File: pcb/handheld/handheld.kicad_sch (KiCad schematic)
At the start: 64 parts, among them J1 Battery, J2 USB_C_Receptacle_USB2.0_16P, J3 Display Output, J4 Speaker ~(3W, 8R), J5 Joystick, J6 Debug, Q1 MMBT3904, SW1 SLW-1678105-6A-N-D, SW10 R, SW2 Reset, SW3 Boot, SW4 Select, SW5 A, SW6 B, SW7 X, SW8 Y, SW9 L, U1 ESP32-S3-WROOM-1, U2 AMS1117-3.3

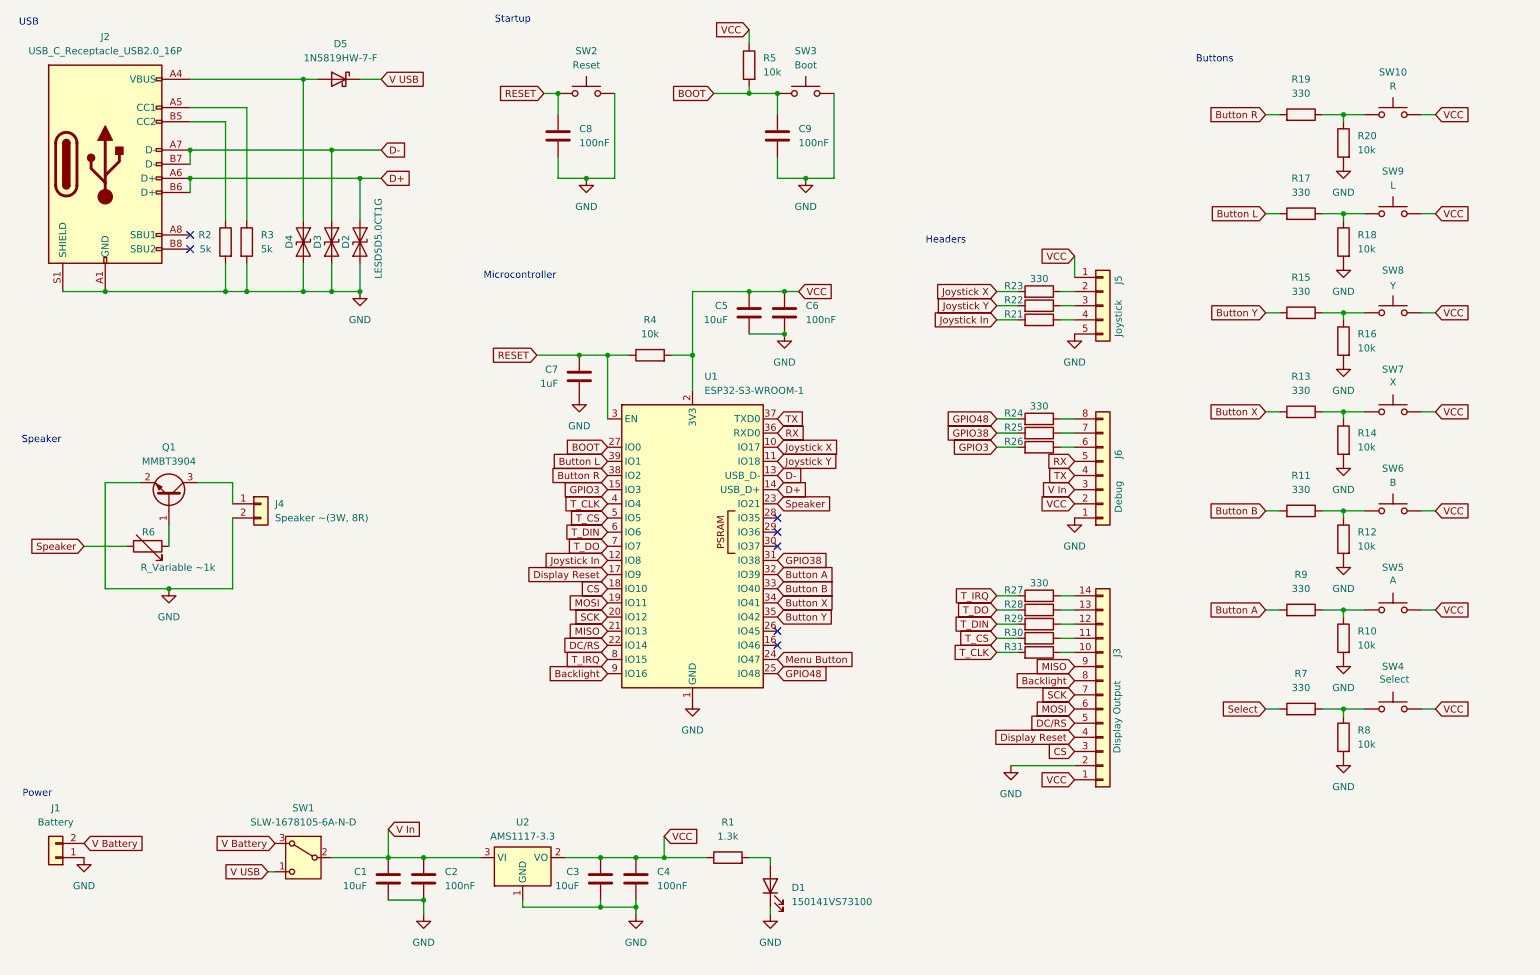
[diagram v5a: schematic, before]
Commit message: Updated symbols and footprints mainly
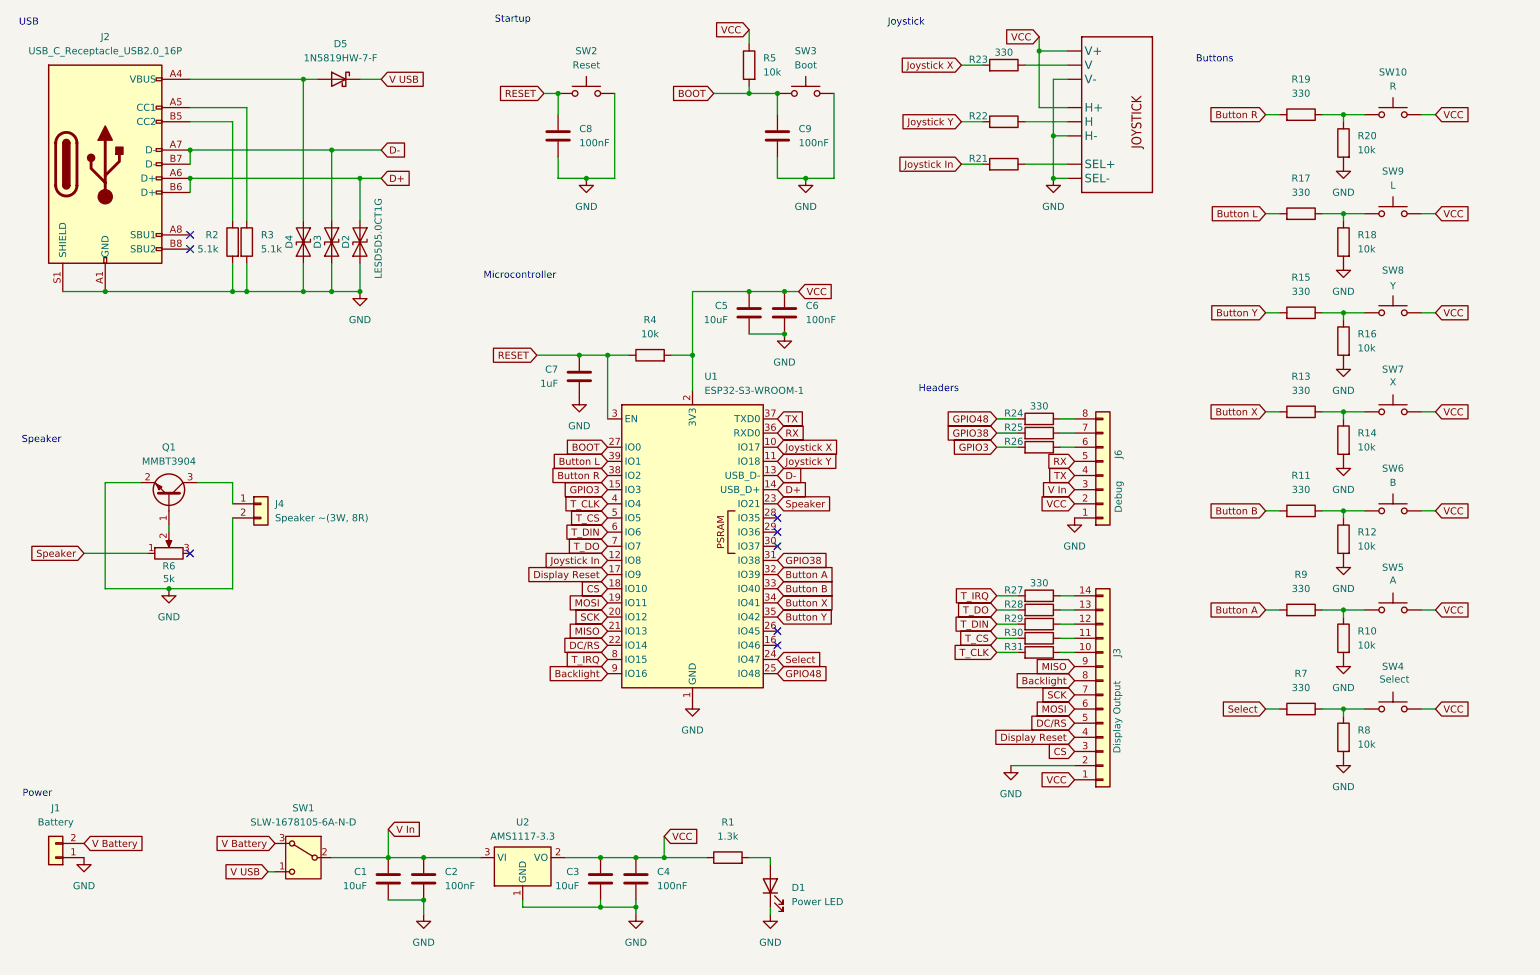
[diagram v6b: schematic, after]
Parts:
- removed J5: Joystick, symbol Connector_Generic:Conn_01x05
- removed R6: R_Variable ~1k, symbol Device:R_Variable
- added R6: 5k, handheld:RES-ADJ-TH_3P-L6.6-W7.0-P2.54-L_3362P, symbol Device:R_Potentiometer
- added U3: ~, handheld:JOYSTICK, symbol handheld_symbols:JOYSTICKPTH
- C1, C2, C3, C4, C5, C6, C7, C8, C9: footprint (none) -> Capacitor_SMD:C_0805_2012Metric
- D1: value 150141VS73100 -> Power LED; footprint (none) -> LED_SMD:LED_0603_1608Metric
- D5: footprint Diode_THT:D_DO-41_SOD81_P10.16mm_Horizontal -> Diode_SMD:D_SOD-123
- J1, J4: footprint (none) -> Connector_PinSocket_2.54mm:PinSocket_1x02_P2.54mm_Horizontal
- J2: footprint (none) -> handheld:USB-SMD_USB-TYPE-C-020
- J3: footprint (none) -> Connector_PinHeader_2.54mm:PinHeader_1x14_P2.54mm_Horizontal
- J6: footprint (none) -> Connector_PinSocket_2.54mm:PinSocket_1x08_P2.54mm_Vertical
- R1, R10, R11, R12, R13, R14, R15, R16, R17, R18, R19, R20, R21, R22, R23, R24, R25, R26, R27, R28, R29, R30, R31, R4, R5, R7, R8, R9: footprint (none) -> Resistor_SMD:R_0805_2012Metric
- R2, R3: value 5k -> 5.1k; footprint (none) -> Resistor_SMD:R_0805_2012Metric
- SW1: footprint Button_Switch_SMD:Nidec_Copal_CAS-120A -> handheld:SW_SLW-1678105-6A-N-D
- SW10, SW2, SW3, SW4, SW5, SW6, SW7, SW8, SW9: footprint (none) -> Button_Switch_THT:SW_TH_Tactile_Omron_B3F-100x
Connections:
- net Menu Button is gone; now on net Select: U1.24 (IO47)
- net GND: now also U3.B2A (SEL-), U3.H3 (H-), U3.V3 (V-)
- net Speaker: now also R6.1
- net VCC: now also U3.H1 (H+), U3.V1 (V+)
- net at Q1.1 (B): now also R6.2
- net at R22.1: now also U3.H2 (H)
- net at R23.1: now also U3.V2 (V)
- net at R21.1: now also U3.B1A (SEL+)
- no-connect marks 7 -> 8
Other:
- note added: "Joystick"
- moved on the sheet: R2, R21, R22, R23

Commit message: Initial PCB routing
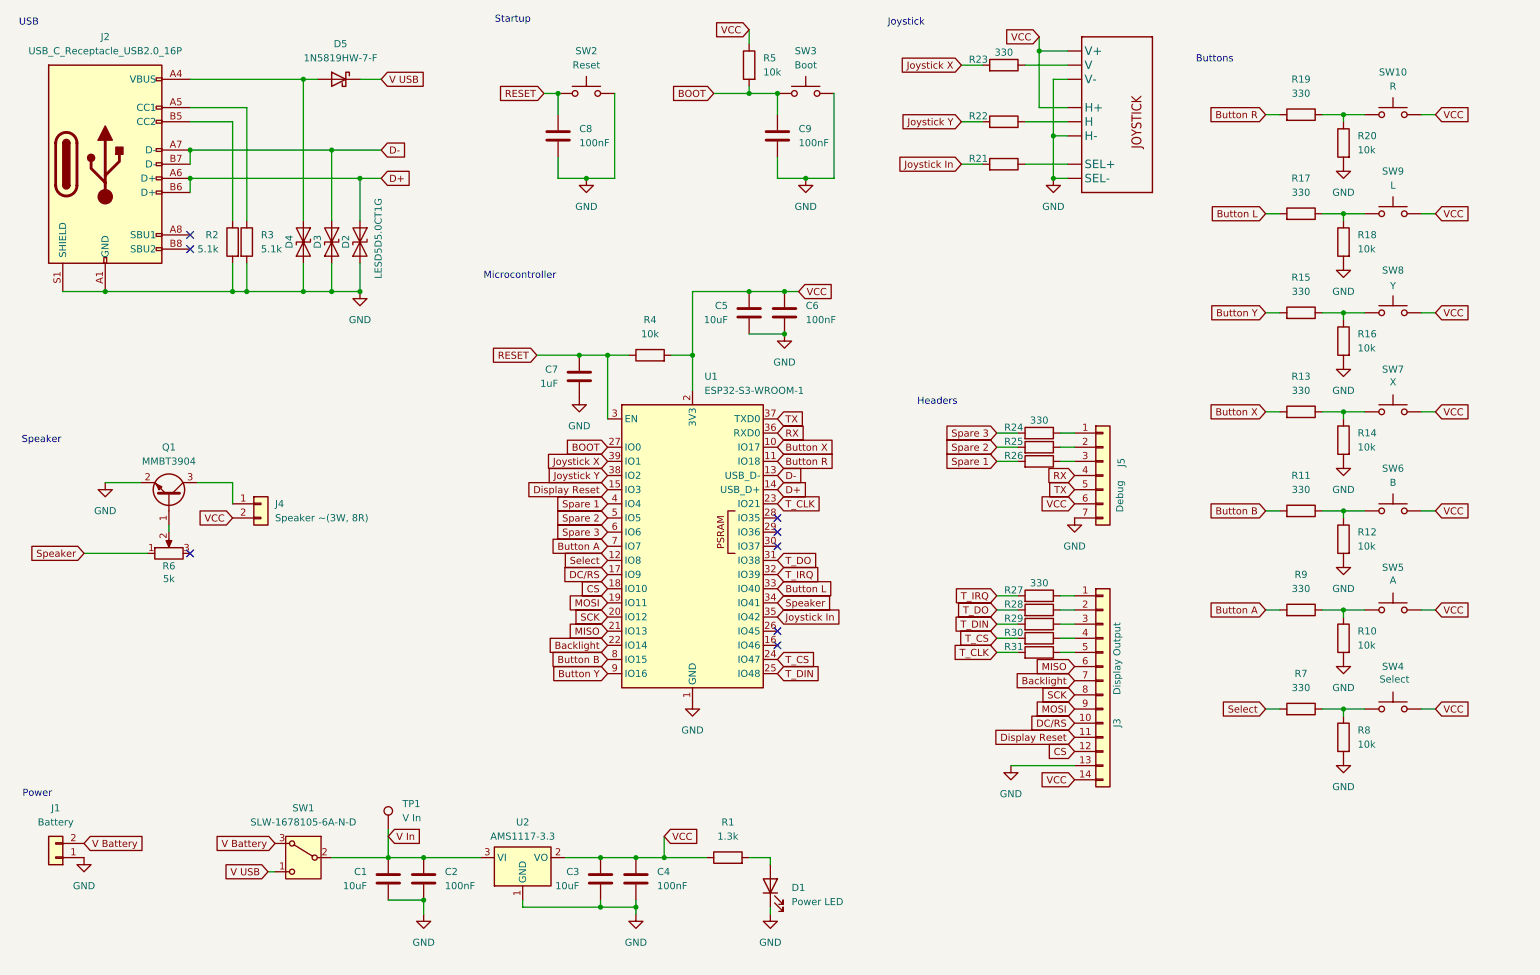
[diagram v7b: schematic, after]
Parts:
- removed J6: Debug, Connector_PinSocket_2.54mm:PinSocket_1x08_P2.54mm_Vertical, symbol Connector_Generic:Conn_01x08
- added J5: Debug, handheld:Header_1x07_P2.54mm_Pads, symbol Connector_Generic:Conn_01x07
- added TP1: V In, handheld:Testpoint, symbol Connector:TestPoint
- R1, R10, R11, R12, R13, R14, R15, R16, R17, R18, R19, R2, R20, R21, R22, R23, R24, R25, R26, R27, R28, R29, R3, R30, R31, R4, R5, R7, R8, R9: footprint Resistor_SMD:R_0805_2012Metric -> Resistor_SMD:R_0603_1608Metric
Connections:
- net Backlight: now also J3.7 (Pin_7), U1.22 (IO14); no longer J3.8 (Pin_8), U1.9 (IO16)
- net Button A: now also U1.7 (IO7); no longer U1.32 (IO39)
- net Button B: now also U1.8 (IO15); no longer U1.33 (IO40)
- net Button L: now also U1.33 (IO40); no longer U1.39 (IO1)
- net Button R: now also U1.11 (IO18); no longer U1.38 (IO2)
- net Button X: now also U1.10 (IO17); no longer U1.34 (IO41)
- net Button Y: now also U1.9 (IO16); no longer U1.35 (IO42)
- net CS: now also J3.12 (Pin_12); no longer J3.3 (Pin_3)
- net DC/RS: now also J3.10 (Pin_10), U1.17 (IO9); no longer J3.5 (Pin_5), U1.22 (IO14)
- net Display Reset: now also J3.11 (Pin_11), U1.15 (IO3); no longer J3.4 (Pin_4), U1.17 (IO9)
- net GND: now also J3.13 (Pin_13), J5.7 (Pin_7); no longer J3.2 (Pin_2), J4.2 (Pin_2)
- net Joystick In: now also U1.35 (IO42); no longer U1.12 (IO8)
- net Joystick X: now also U1.39 (IO1); no longer U1.10 (IO17)
- net Joystick Y: now also U1.38 (IO2); no longer U1.11 (IO18)
- net MISO: now also J3.6 (Pin_6); no longer J3.9 (Pin_9)
- net MOSI: now also J3.9 (Pin_9); no longer J3.6 (Pin_6)
- net RX: now also J5.4 (Pin_4)
- net SCK: now also J3.8 (Pin_8); no longer J3.7 (Pin_7)
- net Select: now also U1.12 (IO8); no longer U1.24 (IO47)
- net Speaker: now also U1.34 (IO41); no longer U1.23 (IO21)
- net TX: now also J5.5 (Pin_5)
- net T_CLK: now also U1.23 (IO21); no longer U1.4 (IO4)
- net T_CS: now also U1.24 (IO47); no longer U1.5 (IO5)
- net T_DIN: now also U1.25 (IO48); no longer U1.6 (IO6)
- net T_DO: now also U1.31 (IO38); no longer U1.7 (IO7)
- net T_IRQ: now also U1.32 (IO39); no longer U1.8 (IO15)
- net V In: now also TP1.1
- net VCC: now also J3.14 (Pin_14), J4.2 (Pin_2), J5.6 (Pin_6); no longer J3.1 (Pin_1)
- net at R28.1: now also J3.2 (Pin_2); no longer J3.13 (Pin_13)
- net at R24.1: now also J5.1 (Pin_1)
- net at R25.1: now also J5.2 (Pin_2)
- net at R31.1: now also J3.5 (Pin_5); no longer J3.10 (Pin_10)
- net at R30.1: now also J3.4 (Pin_4); no longer J3.11 (Pin_11)
- net at R29.1: now also J3.3 (Pin_3); no longer J3.12 (Pin_12)
- net at R27.1: now also J3.1 (Pin_1); no longer J3.14 (Pin_14)
- net at R26.1: now also J5.3 (Pin_3)
- net GPIO3 renamed Spare 1
- net Spare 1: now also U1.4 (IO4); no longer U1.15 (IO3)
- net GPIO38 renamed Spare 2
- net Spare 2: now also U1.5 (IO5); no longer U1.31 (IO38)
- net GPIO48 renamed Spare 3
- net Spare 3: now also U1.6 (IO6); no longer U1.25 (IO48)
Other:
- moved on the sheet: R24, R25, R26

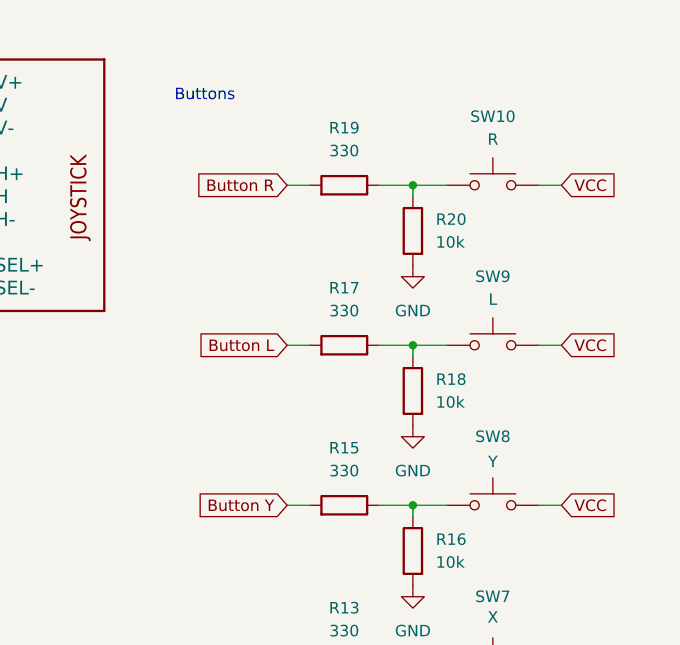
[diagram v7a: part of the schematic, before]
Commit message: Updated components and shrunk width
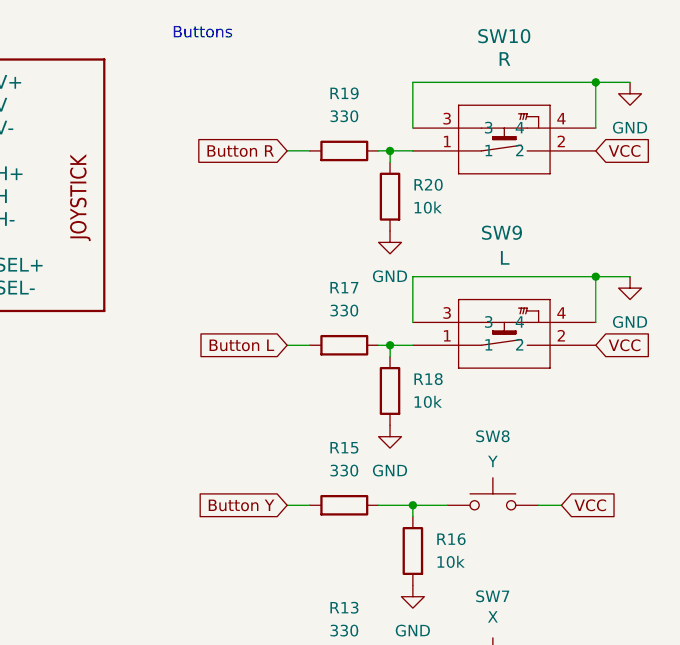
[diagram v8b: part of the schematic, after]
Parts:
- removed SW10: R, Button_Switch_THT:SW_TH_Tactile_Omron_B3F-100x, symbol Switch:SW_Push
- removed SW9: L, Button_Switch_THT:SW_TH_Tactile_Omron_B3F-100x, symbol Switch:SW_Push
- added SW10: R, handheld:SW_B3F-3150_OMR, symbol handheld_symbols:B3F-3152
- added SW9: L, handheld:SW_B3F-3150_OMR, symbol handheld_symbols:B3F-3152
- J1, J4: footprint Connector_PinSocket_2.54mm:PinSocket_1x02_P2.54mm_Horizontal -> handheld:CONN_S2B-PH-K-S_JST
- J5: footprint handheld:Header_1x07_P2.54mm_Pads -> Connector_PinHeader_2.54mm:PinHeader_1x07_P2.54mm_Vertical
- R6: footprint handheld:RES-ADJ-TH_3P-L6.6-W7.0-P2.54-L_3362P -> handheld:PTV09A-4015F-B104_BRN
- SW2, SW3, SW4, SW5, SW6, SW7, SW8: footprint Button_Switch_THT:SW_TH_Tactile_Omron_B3F-100x -> handheld:SW_B3F-1050_OMR
- U3: value ~ -> Joystick Mount
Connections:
- net GND: now also SW10.3, SW10.4, SW9.3, SW9.4
- net VCC: now also SW10.2, SW9.2
- net at R19.1, R20.1: now also SW10.1
- net at R17.1, R18.1: now also SW9.1
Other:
- moved on the sheet: R18, R19, R20
